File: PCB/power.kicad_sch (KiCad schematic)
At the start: 32 parts, among them IC1 NCP333FCT2G, Q1 NMOS, Q2 NMOS, SW1 SW_SPST, U2 BQ297xy, U3 BQ24090DGQ, U6 TPS63001

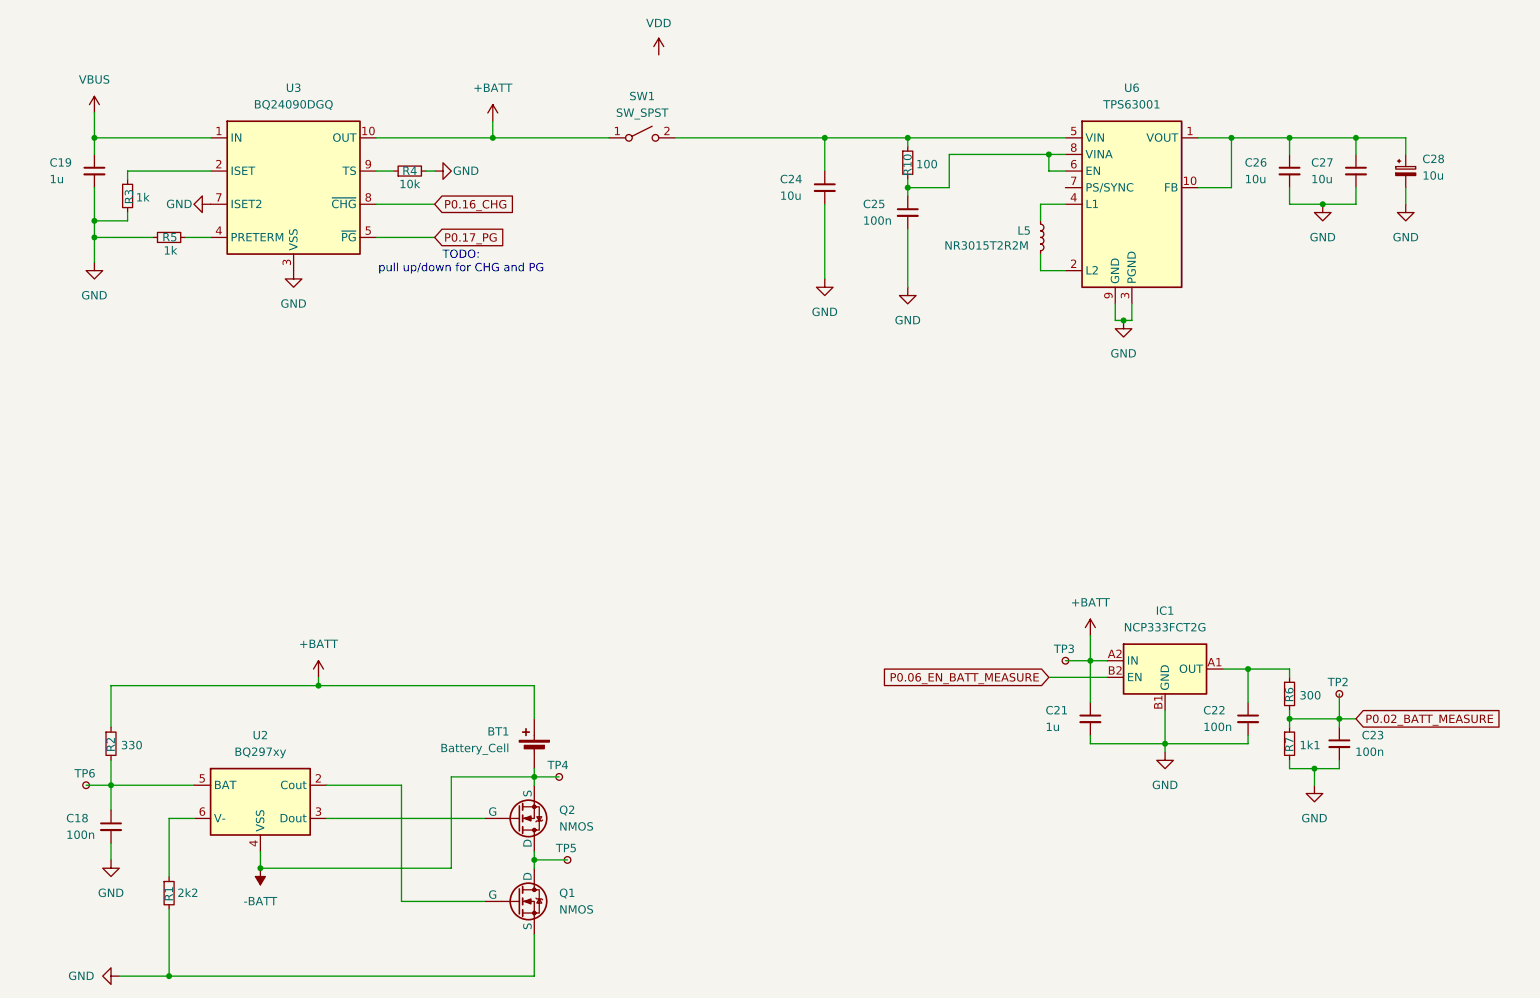
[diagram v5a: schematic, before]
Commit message: redid the pcb layout for a more bigger devboard approach. Added a few more components and the antenna.
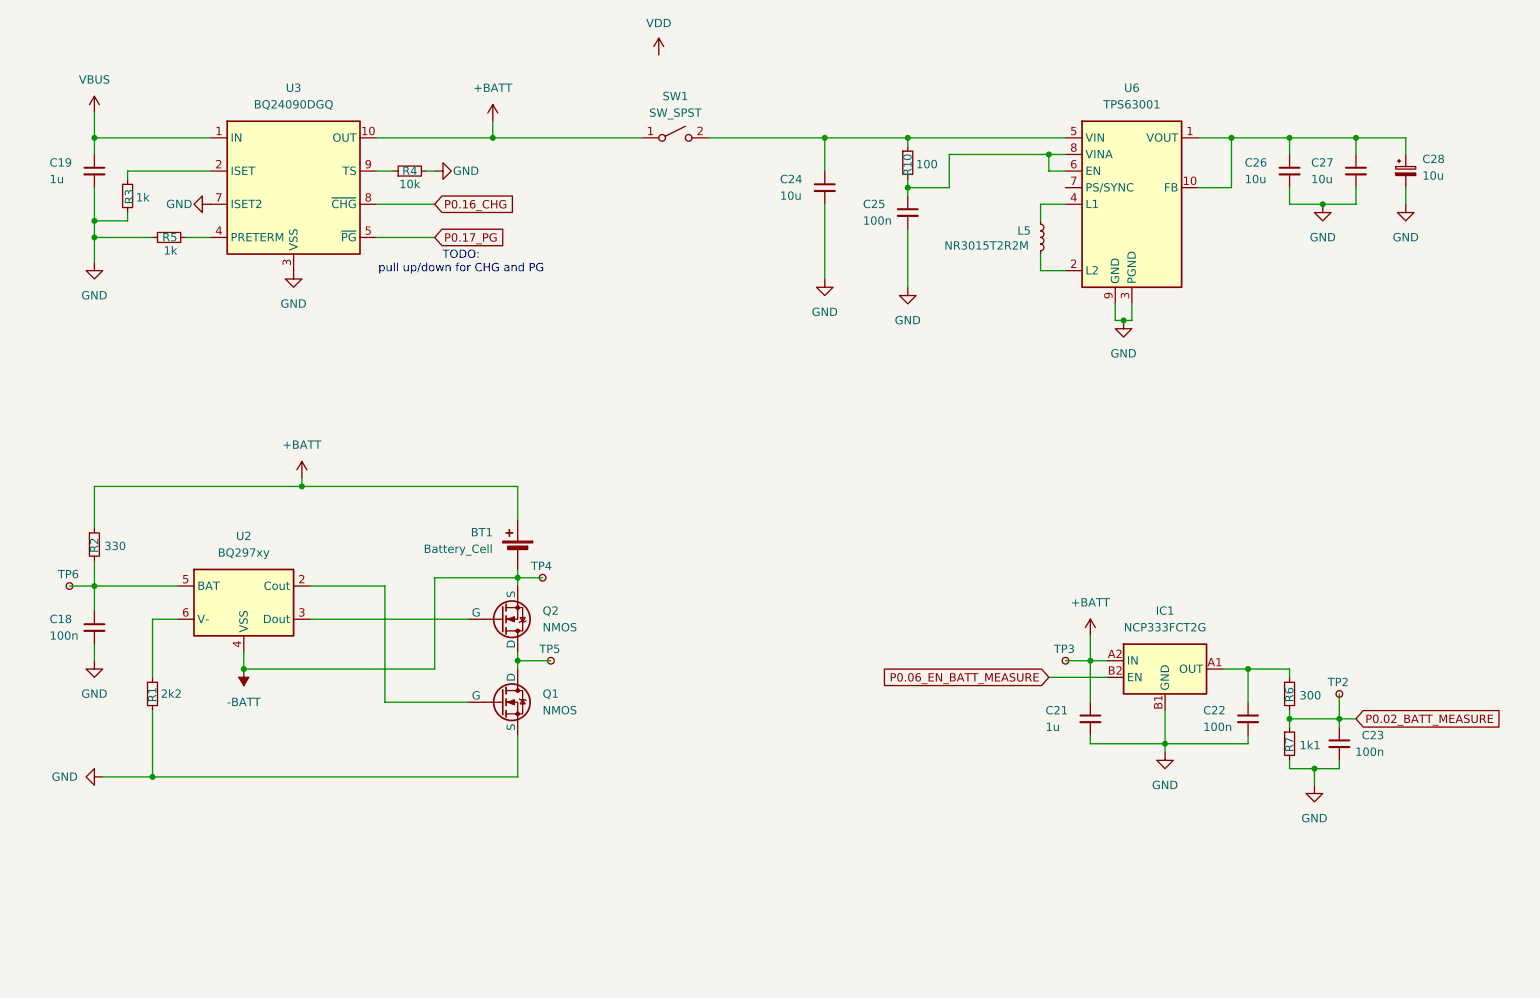
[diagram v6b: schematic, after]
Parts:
- BT1: footprint Connector_JST:JST_PH_B2B-PH-SM4-TB_1x02-1MP_P2.00mm_Vertical -> Connector_JST:JST_PH_S2B-PH-K_1x02_P2.00mm_Horizontal
- C28: footprint (none) -> Capacitor_SMD:CP_Elec_5x4.4
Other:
- moved on the sheet: BT1, C18, Q1, Q2, R1, R2, SW1, TP4, TP5, TP6, U2

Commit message: Added more Components
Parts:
- removed TP3, TP4: TestPoint_Small, TestPoint:TestPoint_Pad_D1.0mm, symbol Connector:TestPoint_Small
- added J5: BATT, Connector_PinHeader_2.54mm:PinHeader_1x02_P2.54mm_Vertical, symbol Connector:Conn_01x02_Pin
- added JP1, JP2: SolderJumper_3_Bridged12, Jumper:SolderJumper-3_P1.3mm_Bridged12_RoundedPad1.0x1.5mm, symbol Jumper:SolderJumper_3_Bridged12
- added TP8: TestPoint_Small, TestPoint:TestPoint_Pad_D1.0mm, symbol Connector:TestPoint_Small
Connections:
- net +BATT: now also J5.2 (Pin_2); no longer BT1.1 (+), R2.1
- net GND: now also JP2.2 (C)
- net P0.06_EN_BATT_MEASURE: now also TP8.1
- net +3.3V: now reaches C26.1, C27.1, C28.1, U6.1 (VOUT), U6.10 (FB)
- net VCC: now reaches C24.1, R10.1, SW1.2 (B), U6.5 (VIN)
- net VINA: now reaches C25.1, R10.2, U6.8 (VINA)
- net VINA: now also JP1.3 (B), JP2.3 (B); no longer U6.6 (EN)
- net PS: now reaches U6.7 (PS/SYNC)
- net PS: now also JP2.1 (A)
- new net: BT1.1 (+), J5.1 (Pin_1), R2.1
- new net EN: JP1.1 (A), U6.6 (EN)
- new net P0.05_EN_DCDC: JP1.2 (C)
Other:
- moved on the sheet: SW1

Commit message: Continued on Devboard
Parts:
- removed J5: BATT, Connector_PinHeader_2.54mm:PinHeader_1x02_P2.54mm_Vertical, symbol Connector:Conn_01x02_Pin
- removed SW1: SW_SPST, symbol Switch:SW_SPST
- added SW1: MK-12C02-G020, G-Switch:SW-SMD_MK-12C02-G020, symbol G-Switch:MK-12C02-G020
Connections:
- net +BATT: now also BT1.1 (+), R2.1, SW1.2
- net VCC: now also SW1.3
- new net: SW1.4, SW1.5
- new net: SW1.6, SW1.7
- no-connect marks 0 -> 1
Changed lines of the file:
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@@
 	)
 	(junction
+		(at 151.13 49.53)
+		(diameter 0)
+		(color 0 0 0 0)
+	)
+	(junction
 		(at 115.57 116.84)
 		(diameter 0)
@@
 	)
 	(junction
+		(at 111.76 49.53)
+		(diameter 0)
+		(color 0 0 0 0)
+	)
+	(junction
 		(at 50.8 49.53)
 		(diameter 0)
@@
 	)
 	(junction
-		(at 111.76 49.53)
-		(diameter 0)
-		(color 0 0 0 0)
-	)
-	(junction
 		(at 251.46 49.53)
 		(diameter 0)
@@
 	)
 	(junction
-		(at 151.13 49.53)
-		(diameter 0)
-		(color 0 0 0 0)
-	)
-	(junction
 		(at 199.39 132.08)
 		(diameter 0)
 		(color 0 0 0 0)
 	)
+	(no_connect
+		(at 127 46.99)
+	)
 	(wire
 		(pts
@@
 	(wire
 		(pts
+			(xy 82.55 93.98) (xy 82.55 102.87)
+		)
+		(stroke
+			(width 0)
+			(type default)
+		)
+	)
+	(wire
+		(pts
 			(xy 102.87 116.84) (xy 115.57 116.84)
 		)
@@
 	(wire
 		(pts
+			(xy 132.08 49.53) (xy 111.76 49.53)
+		)
+		(stroke
+			(width 0)
+			(type default)
+		)
+	)
+	(wire
+		(pts
 			(xy 46.99 118.11) (xy 50.8 118.11)
 		)
@@
 	(wire
 		(pts
-			(xy 199.39 129.54) (xy 199.39 132.08)
+			(xy 137.16 46.99) (xy 137.16 49.53)
 		)
 		(stroke
@@
 	(wire
 		(pts
-			(xy 50.8 114.3) (xy 50.8 118.11)
+			(xy 199.39 129.54) (xy 199.39 132.08)
 		)
 		(stroke
@@
 	(wire
 		(pts
-			(xy 219.71 57.15) (xy 224.79 57.15)
+			(xy 50.8 114.3) (xy 50.8 118.11)
 		)
 		(stroke
@@
 	(wire
 		(pts
-			(xy 243.84 49.53) (xy 243.84 52.07)
+			(xy 219.71 57.15) (xy 224.79 57.15)
 		)
 		(stroke
@@
 	(wire
 		(pts
-			(xy 140.97 49.53) (xy 151.13 49.53)
+			(xy 243.84 49.53) (xy 243.84 52.07)
 		)
 		(stroke
@@
 	(wire
 		(pts
-			(xy 111.76 49.53) (xy 130.81 49.53)
+			(xy 124.46 46.99) (xy 124.46 52.07)
 		)
 		(stroke
@@
 	(wire
 		(pts
-			(xy 82.55 93.98) (xy 82.55 97.79)
+			(xy 95.25 118.11) (xy 95.25 135.89)
 		)
 		(stroke
@@
 	(wire
 		(pts
-			(xy 95.25 118.11) (xy 95.25 135.89)
+			(xy 233.68 59.69) (xy 238.76 59.69)
 		)
 		(stroke
@@
 	(wire
 		(pts
-			(xy 233.68 59.69) (xy 238.76 59.69)
+			(xy 233.68 49.53) (xy 233.68 52.07)
 		)
 		(stroke
@@
 	(wire
 		(pts
-			(xy 233.68 49.53) (xy 233.68 52.07)
+			(xy 175.26 49.53) (xy 162.56 49.53)
 		)
 		(stroke
@@
 	(wire
 		(pts
-			(xy 175.26 49.53) (xy 162.56 49.53)
+			(xy 50.8 57.15) (xy 50.8 62.23)
 		)
 		(stroke
@@
 	(wire
 		(pts
-			(xy 50.8 57.15) (xy 50.8 62.23)
+			(xy 151.13 45.72) (xy 151.13 49.53)
 		)
 		(stroke
@@
 	(wire
 		(pts
-			(xy 151.13 45.72) (xy 151.13 49.53)
+			(xy 181.61 52.07) (xy 184.15 52.07)
 		)
 		(stroke
@@
 	(wire
 		(pts
-			(xy 181.61 52.07) (xy 184.15 52.07)
+			(xy 139.7 46.99) (xy 139.7 52.07)
+		)
+		(stroke
+			(width 0)
+			(type default)
+		)
+	)
+	(wire
+		(pts
+			(xy 142.24 46.99) (xy 142.24 52.07)
 		)
 		(stroke
@@
 	(wire
 		(pts
-			(xy 82.55 100.33) (xy 82.55 102.87)
+			(xy 121.92 46.99) (xy 121.92 52.07)
 		)
 		(stroke
@@
 	(wire
 		(pts
+			(xy 137.16 49.53) (xy 151.13 49.53)
+		)
+		(stroke
+			(width 0)
+			(type default)
+		)
+	)
+	(wire
+		(pts
 			(xy 115.57 129.54) (xy 115.57 130.81)
 		)
@@
 	(wire
 		(pts
+			(xy 121.92 52.07) (xy 124.46 52.07)
+		)
+		(stroke
+			(width 0)
+			(type default)
+		)
+	)
+	(wire
+		(pts
 			(xy 55.88 62.23) (xy 50.8 62.23)
 		)
@@
 	(wire
 		(pts
+			(xy 132.08 46.99) (xy 132.08 49.53)
+		)
+		(stroke
+			(width 0)
+			(type default)
+		)
+	)
+	(wire
+		(pts
 			(xy 162.56 59.69) (xy 162.56 71.12)
 		)
@@
 	(wire
 		(pts
+			(xy 139.7 52.07) (xy 142.24 52.07)
+		)
+		(stroke
+			(width 0)
+			(type default)
+		)
+	)
+	(wire
+		(pts
 			(xy 227.33 140.97) (xy 227.33 142.24)
 		)
@@
 	)
 	(symbol
-		(lib_id "Connector:Conn_01x02_Pin")
-		(at 87.63 100.33 180)
-		(unit 1)
-		(exclude_from_sim no)
-		(in_bom yes)
-		(on_board yes)
-		(dnp no)
-		(fields_autoplaced yes)
-		(property "Reference" "J5"
-			(at 88.9 97.7899 0)
-			(effects
-				(font
-					(size 1.27 1.27)
-				)
-				(justify right)
-			)
-		)
-		(property "Value" "BATT"
-			(at 88.9 100.3299 0)
-			(effects
-				(font
-					(size 1.27 1.27)
-				)
-				(justify right)
-			)
-		)
-		(property "Footprint" "Connector_PinHeader_2.54mm:PinHeader_1x02_P2.54mm_Vertical"
-			(at 87.63 100.33 0)
-			(effects
-				(font
-					(size 1.27 1.27)
-				)
-				(hide yes)
-			)
-		)
-		(property "Datasheet" "~"
-			(at 87.63 100.33 0)
-			(effects
-				(font
-					(size 1.27 1.27)
-				)
-				(hide yes)
-			)
-		)
-		(property "Description" "Generic connector, single row, 01x02, script generated"
-			(at 87.63 100.33 0)
-			(effects
-				(font
-					(size 1.27 1.27)
-				)
-				(hide yes)
-			)
-		)
-		(pin "1"
-		)
-		(pin "2"
-		)
-		(instances
-			(project "Plant_Thing"
-				(path "/3604ffe7-6852-4862-a71a-75c04c0147cb/0dd4cb45-5326-4750-ad2c-3aa13f0ce268"
-					(reference "J5")
-					(unit 1)
-				)
-			)
-		)
-	)
-	(symbol
 		(lib_id "power:GND")
 		(at 222.25 92.71 0)
@@
 	)
 	(symbol
-		(lib_id "Switch:SW_SPST")
-		(at 135.89 49.53 0)
+		(lib_id "G-Switch:MK-12C02-G020")
+		(at 132.08 41.91 0)
 		(unit 1)
 		(exclude_from_sim no)
@@
 		(fields_autoplaced yes)
 		(property "Reference" "SW1"
-			(at 135.89 43.18 0)
+			(at 132.08 31.75 0)
 			(effects
 				(font
@@
 			)
 		)
-		(property "Value" "SW_SPST"
-			(at 135.89 45.72 0)
+		(property "Value" "MK-12C02-G020"
+			(at 132.08 34.29 0)
 			(effects
 				(font
@@
 			)
 		)
-		(property "Footprint" ""
-			(at 135.89 49.53 0)
+		(property "Footprint" "G-Switch:SW-SMD_MK-12C02-G020"
+			(at 132.08 54.61 0)
 			(effects
 				(font
@@
 			)
 		)
-		(property "Datasheet" "~"
-			(at 135.89 49.53 0)
+		(property "Datasheet" "https://lcsc.com/product-detail/Toggle-Switches_G-Switch-MK-12C02-G020_C963206.html"
+			(at 132.08 57.15 0)
 			(effects
 				(font
@@
 			)
 		)
-		(property "Description" "Single Pole Single Throw (SPST) switch"
-			(at 135.89 49.53 0)
+		(property "Description" ""
+			(at 132.08 41.91 0)
 			(effects
 				(font
@@
 			)
 		)
-		(pin "1"
+		(property "LCSC Part" "C963206"
+			(at 132.08 59.69 0)
+			(effects
+				(font
+					(size 1.27 1.27)
+				)
+				(hide yes)
+			)
+		)
+		(pin "3"
+		)
+		(pin "7"
+		)
+		(pin "6"
+		)
+		(pin "5"
+		)
+		(pin "4"
 		)
 		(pin "2"
 		)
+		(pin "1"
+		)
 		(instances
